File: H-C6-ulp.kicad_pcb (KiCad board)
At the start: 4 copper layers, 58.5 x 33 mm, 81 parts, among them IC1 W25Q80DVSSIG, J1 USB_C_Receptacle_USB2.0, J2 AFC24-S24FIC-00, J3 SM02B-SRSS-TB(LF)(SN), J4 SM04B-SRSS-TB_LF__SN_, J5 OLED, Q1 Si1308, Q2 Si2301CDS, SW1 SW_Push_Dual, SW2 SW_Push_Dual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

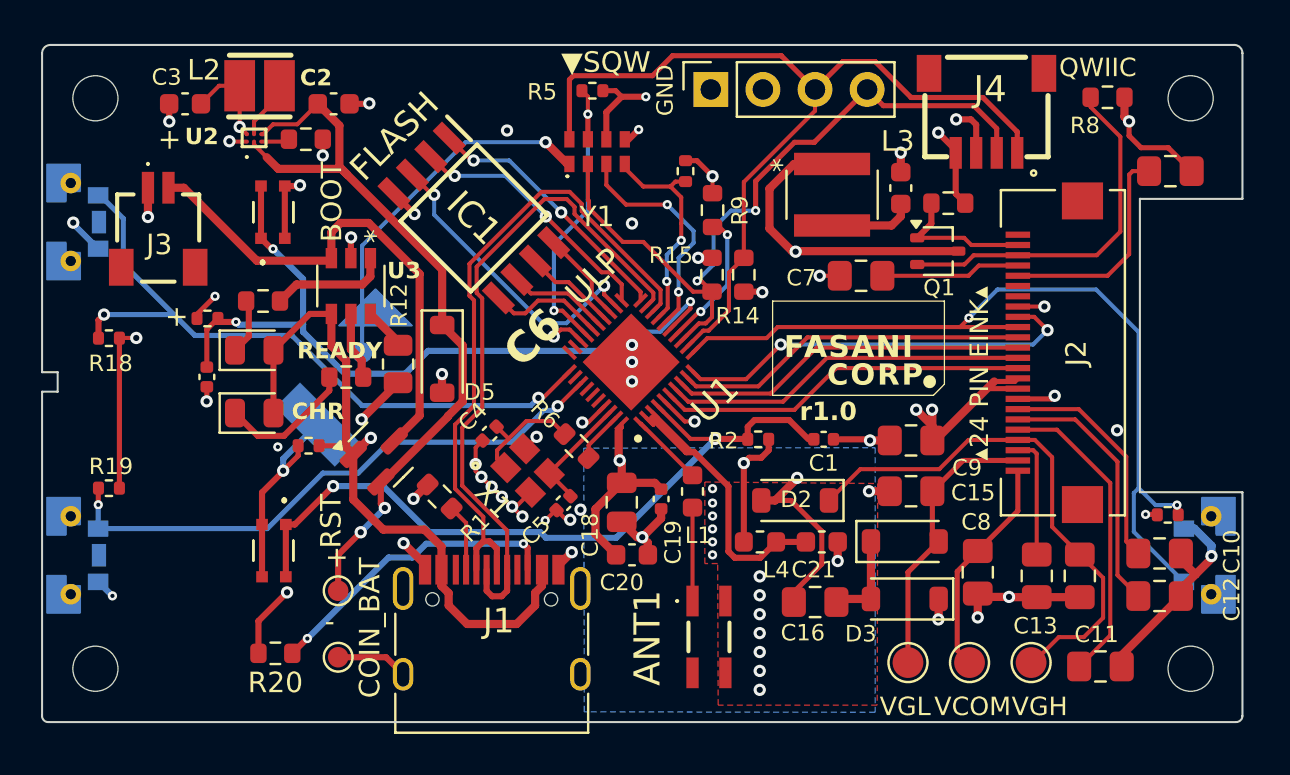
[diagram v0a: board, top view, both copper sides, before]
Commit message: Test with external flash
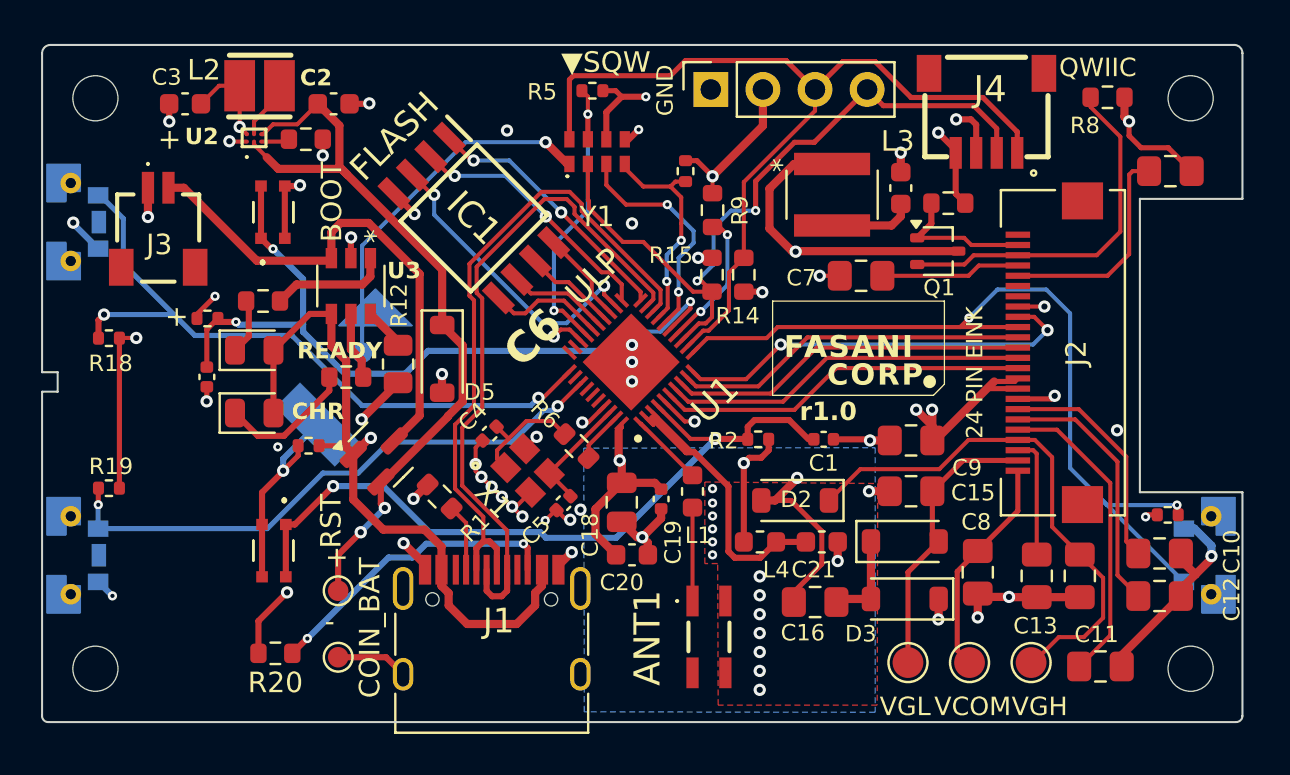
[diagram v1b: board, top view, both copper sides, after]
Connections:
- J5 pad 2: +3.3V -> VDD33
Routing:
- net VDD33: track 99.4 -> 104.8 mm
- net +3.3V: track 5.10 -> 0.00 mm
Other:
- board text added: "24 PIN EINK"
- board text removed: "▴24 PIN EINK▴"

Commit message: 1.1 ready for review
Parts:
- removed IC1: W25Q80DVSSIG, footprints:SOIC127P790X216-8N-FLASH
- removed R5: 10 K, Resistor_SMD:R_0402_1005Metric
- removed TP4: COIN BAT +, TestPoint:TestPoint_Pad_D1.0mm
- removed TP5: COIN BAT -, TestPoint:TestPoint_Pad_D1.0mm
- added TP10: RX, TestPoint:TestPoint_Pad_D1.0mm, F.Cu at (127.7, 49.3)
- added TP6: 21, TestPoint:TestPoint_Pad_D1.0mm, F.Cu at (117.0, 68.0)
- added TP7: 22, TestPoint:TestPoint_Pad_D1.0mm, F.Cu at (117.0, 71.6)
- added TP8: 23, TestPoint:TestPoint_Pad_D1.0mm, F.Cu at (117.0, 75.2)
- added TP9: TX, TestPoint:TestPoint_Pad_D1.0mm, F.Cu at (130.2, 49.3)
- U1: value ESP32-C6 -> ESP32-C6FH4; footprint footprints:C6_QFN40P500X500X90-41N-D -> Package_DFN_QFN:QFN-32-1EP_5x5mm_P0.5mm_EP3.6x3.6mm
- moved U1 0.48 mm to (138.5, 63.5)
- moved R6 0.28 mm to (135.8, 67.3)
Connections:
- R19 pad 1: SW20 -> SW19
- U1 pad 16: /RTC_INT -> /USB_D-
- U1 pad 17: /RTC_EVI -> /USB_D+
- U1 pad 18: /USB_D- -> /RTC_EVI
- U1 pad 19: /USB_D+ -> /RTC_INT
- U1 pad 20: SPICS0 -> VDD33
- U1 pad 21: SPI_D1 -> /IO_TX
- U1 pad 22: SPI_D2 -> /IO_RX
- U1 pad 23: SPIVDD -> SW18
- U1 pad 24: SPI_D3 -> SW19
- U1 pad 25: SPICLK -> /RTC_SQW
- U1 pad 26: SPI_D0 -> /IO_21
- U1 pad 27: /RTC_SQW -> /IO_22
- U1 pad 28: VDD33 -> /IO_23
- U1 pad 29: unconnected-(U1-U0TXD/GPIO16/FSPICS0-Pad29) -> VDD33
- U1 pad 30: unconnected-(U1-U0RXD/GPIO17/FSPICS1-Pad30) -> Net-(U1-XTAL_N)
- U1 pad 31: SW18 -> Net-(U1-XTAL_P)
- U1 pad 32: unconnected-(U1-GPIO19/SDIO_CLK/FSPICS3-Pad32) -> VDD33
- U1 pad 33: SW20 -> GND
- U6 pad 2: SW20 -> SW19
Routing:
- net SW19: track 0.00 -> 30.5 mm, vias 0 -> 2
- net SW20: track 28.5 -> 0.00 mm, vias 2 -> 0
- net /IO_23: track 0.00 -> 23.9 mm, vias 0 -> 2
- net /IO_22: track 0.00 -> 22.3 mm, vias 0 -> 2
- net /IO_21: track 0.00 -> 21.5 mm, vias 0 -> 2
- net /IO_RX: track 0.00 -> 17.5 mm, vias 0 -> 2
- net /IO_TX: track 0.00 -> 15.9 mm, vias 0 -> 2
- net SPI_D2: track 14.9 -> 0.00 mm, vias 2 -> 0
- net SPICS0: track 12.8 -> 0.00 mm, vias 2 -> 0
- net SPI_D1: track 12.7 -> 0.00 mm, vias 2 -> 0
- net /RTC_SQW: track 14.9 -> 21.4 mm
- net VDD: track 37.9 -> 31.7 mm, vias 2 -> 0
- net SPI_D0: track 5.74 -> 0.00 mm
- net BOOT: track 37.8 -> 42.9 mm
- net SPICLK: track 4.87 -> 0.00 mm
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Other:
- board text added: "21"
- board text added: "22"
- board text added: "23"
- board text added: "RX 17"
- board text added: "Rev 1.1"
- board text added: "TX 16"
- board text removed: "-"
- board text removed: "COIN_BAT"
- board text removed: "FLASH"
- board text removed: "Rev 1.0"
- board text removed: "r1.0"

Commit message: Cleanup
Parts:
- moved R4 1.35 mm to (141.3, 55.1)
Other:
- board text removed: "▼SQW"
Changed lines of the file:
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@@
   )
   (footprint "Resistor_SMD:R_0402_1005Metric" (layer "F.Cu")
-    (at 141.36 53.75 -90)
+    (at 141.3 55.1 -90)
     (descr "Resistor SMD 0402 (1005 Metric), square (rectangular) end terminal, IPC_7351 nominal, (Body size source: IPC-SM-782 page 72, https://www.pcb-3d.com/wordpress/wp-content/uploads/ipc-sm-782a_amendment_1_and_2.pdf), generated with kicad-footprint-generator")
     (tags "resistor")
@@
     (effects (font (size 1 1) (thickness 0.1)) (justify left bottom))
   )
-  (gr_text "▼SQW" (at 135.3 49.03) (layer "F.SilkS" knockout)
-    (effects (font (size 1 1) (thickness 0.1)) (justify left bottom))
-  )
-  (gr_text "GND" (at 140.95 52.65) (layer "F.SilkS")
+  (gr_text "GND" (at 141.2 53.9 45) (layer "F.SilkS")
     (effects (font (size 0.8 0.8) (thickness 0.1)) (justify left bottom))
   )
@@
     (effects (font (size 1 1) (thickness 0.1)) (justify left bottom))
   )
-  (gr_text "3V3" (at 143.45 53.9 45) (layer "F.SilkS")
+  (gr_text "3V3" (at 143.2 53.9 45) (layer "F.SilkS")
     (effects (font (size 0.8 0.8) (thickness 0.1)) (justify left bottom))
   )
@@
   (segment (start 138.25 68.94) (end 139.86 68.94) (width 0.4) (layer "F.Cu") (net 6))
   (segment (start 144.2 67.98) (end 144.46 67.72) (width 0.3) (layer "F.Cu") (net 6))
-  (segment (start 141.915 53.24) (end 142.675 54) (width 0.25) (layer "F.Cu") (net 6))
   (segment (start 156.4 64) (end 157.4044 64) (width 0.25) (layer "F.Cu") (net 6))
   (segment (start 136.942893 65.392893) (end 136.457906 65.87788) (width 0.2) (layer "F.Cu") (net 6))
@@
   (segment (start 154.547702 51.227298) (end 155.267298 51.227298) (width 0.3) (layer "F.Cu") (net 6))
   (segment (start 119.98 51.95125) (end 119.98 51.94375) (width 0.2) (layer "F.Cu") (net 6))
+  (segment (start 142.675 54.825) (end 141.535 54.825) (width 0.2) (layer "F.Cu") (net 6))
   (segment (start 136.924517 61.574517) (end 134.45 59.1) (width 0.25) (layer "F.Cu") (net 6))
   (segment (start 137.85 66.607106) (end 138.003553 66.453553) (width 0.2) (layer "F.Cu") (net 6))
   (segment (start 138.15 67.85) (end 138.15 67.55) (width 0.4) (layer "F.Cu") (net 6))
-  (segment (start 141.36 53.24) (end 141.915 53.24) (width 0.25) (layer "F.Cu") (net 6))
   (segment (start 153.3875 66.875) (end 153.3875 65.3875) (width 0.4) (layer "F.Cu") (net 6))
   (segment (start 144.2 59.625) (end 145.075 59.625) (width 0.3) (layer "F.Cu") (net 6))
@@
   (segment (start 164.35 70.5) (end 163.88 70.5) (width 0.25) (layer "F.Cu") (net 6))
   (segment (start 163.88 70.5) (end 163.78 70.6) (width 0.25) (layer "F.Cu") (net 6))
+  (segment (start 141.535 54.825) (end 141.3 54.59) (width 0.2) (layer "F.Cu") (net 6))
   (segment (start 144.46 67.72) (end 145.045 67.72) (width 0.3) (layer "F.Cu") (net 6))
   (segment (start 153.525 66.875) (end 156.4 64) (width 0.4) (layer "F.Cu") (net 6))
@@
   (segment (start 120.68 52.31125) (end 121.9125 52.31125) (width 0.2) (layer "F.Cu") (net 48))
   (segment (start 138.4 55.2) (end 137.75 55.85) (width 0.25) (layer "F.Cu") (net 49))
+  (segment (start 138.4 53.6) (end 140.41 55.61) (width 0.2) (layer "F.Cu") (net 49))
   (segment (start 136.3 57.4) (end 136.3 59.51741) (width 0.25) (layer "F.Cu") (net 49))
-  (segment (start 139.3 54.5) (end 138.4 53.6) (width 0.2) (layer "F.Cu") (net 49))
+  (segment (start 140.41 55.61) (end 141.3 55.61) (width 0.2) (layer "F.Cu") (net 49))
   (segment (start 136.3 59.51741) (end 137.65 60.86741) (width 0.25) (layer "F.Cu") (net 49))
-  (segment (start 140.625 54.5) (end 140.865 54.26) (width 0.2) (layer "F.Cu") (net 49))
-  (segment (start 140.865 54.26) (end 141.36 54.26) (width 0.2) (layer "F.Cu") (net 49))
-  (segment (start 140.625 54.5) (end 139.3 54.5) (width 0.2) (layer "F.Cu") (net 49))
   (segment (start 138.4 53.4) (end 138.4 55.2) (width 0.25) (layer "F.Cu") (net 49))
   (via (at 137.75 55.85) (size 0.6) (drill 0.3) (layers "F.Cu" "B.Cu") (net 49))

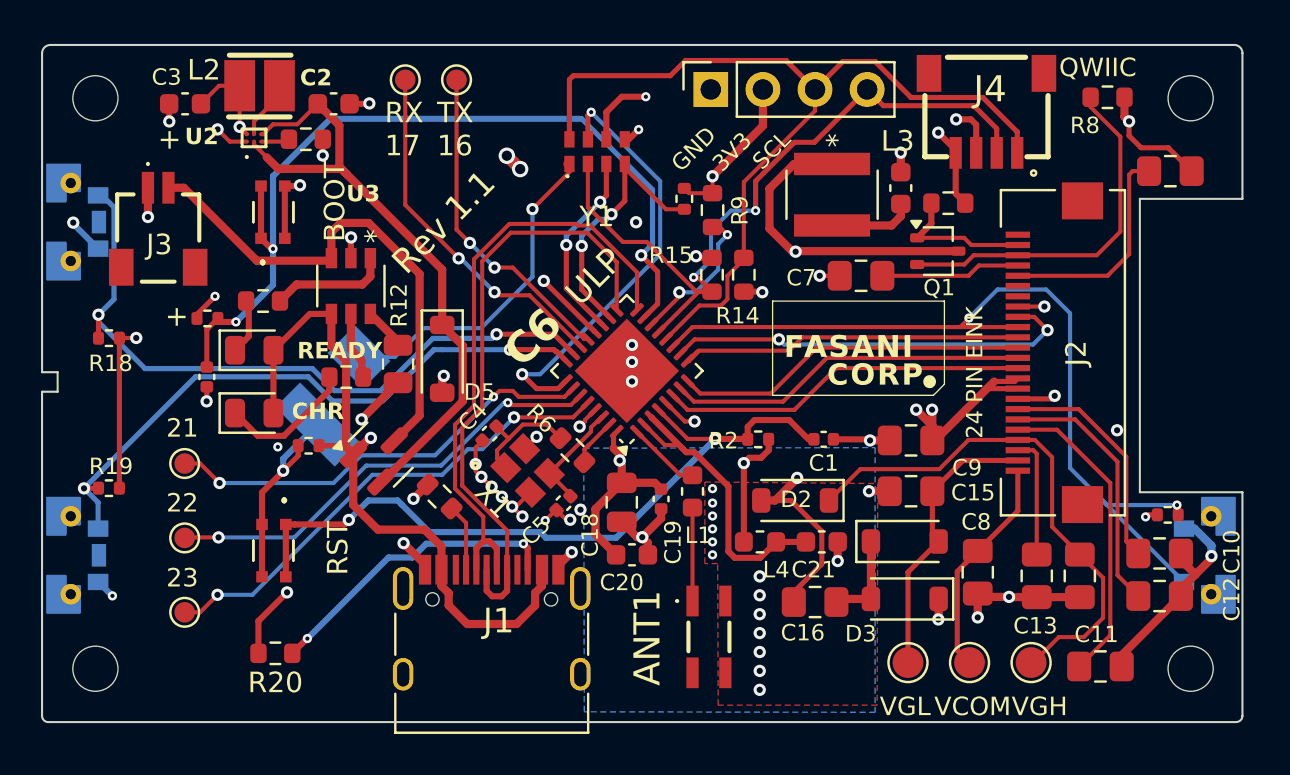
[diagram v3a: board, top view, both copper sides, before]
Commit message: Saving 1.1 state before making it 51 mm
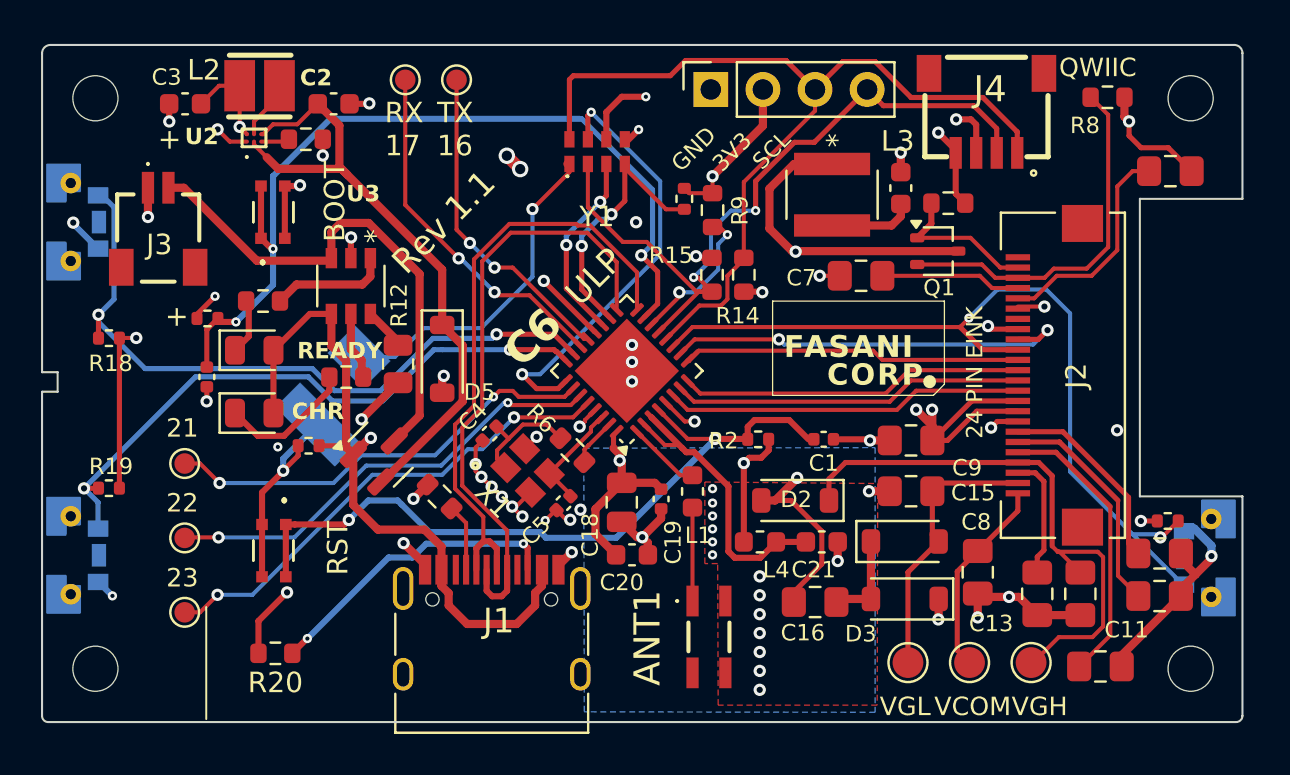
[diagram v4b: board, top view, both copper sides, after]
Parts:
- moved J2 1.10 mm to (159.8, 63.7)
- moved C13 0.88 mm to (158.5, 74.3)
- moved C14 0.88 mm to (160.6, 74.3)
- moved R17 0.30 mm to (164.9, 70.8)
- moved U5 0.13 mm to (166.5, 72.6)
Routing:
- net VDD33: track 107.4 -> 110.0 mm
- net Net-(C10-Pad2): track 11.2 -> 8.98 mm
- net PREVGH: track 25.8 -> 27.8 mm
- net Net-(C12-Pad2): track 12.7 -> 11.1 mm
- net unconnected-(J2-Pad19): track 0.00 -> 1.30 mm, vias 0 -> 1
- net /EPD_RST: track 43.6 -> 42.4 mm
- net Net-(C11-Pad2): track 15.2 -> 14.0 mm
- net /VCOM: track 10.8 -> 9.72 mm
- net Net-(D1-A): track 13.9 -> 12.9 mm
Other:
- outline, holes or cut-outs redrawn

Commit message: Rel 1.1 ready
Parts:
- R7: footprint Resistor_SMD:R_0603_1608Metric -> Resistor_SMD:R_0402_1005Metric
- moved SW2 17.2 mm to (118.2, 72.7), turned to -90 degrees
- moved R18 12.9 mm to (121.5, 52.0)
- moved TP6 10.5 mm to (123.3, 76.3)
- moved C2 10.0 mm to (129.6, 58.9), turned to -90 degrees
- moved TP7 8.80 mm to (121.9, 78.9)
- moved TP8 8.70 mm to (124.8, 78.9)
- moved C3 7.34 mm to (124.3, 50.8), turned to 90 degrees
- moved L2 6.88 mm to (127.4, 50.5)
- moved R3 6.88 mm to (129.7, 53.1)
- moved U2 6.88 mm to (127.2, 53.0)
- moved R16 6.01 mm to (119.3, 66.8), turned to 90 degrees
- moved H1 5.40 mm to (118.0, 50.2)
- moved H3 5.40 mm to (118.0, 78.0)
- moved U4 5.08 mm to (117.0, 55.6)
- moved U6 5.08 mm to (117.0, 71.9)
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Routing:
- net VDD33: track 110.0 -> 97.2 mm, vias 21 -> 18
- net BOOT: track 42.9 -> 52.8 mm, vias 3 -> 2
- net VDD: track 31.7 -> 24.4 mm
- net VBUS: track 40.1 -> 47.0 mm
- net GND: track 84.7 -> 90.0 mm, vias 57 -> 55
- net SW19: track 30.5 -> 25.6 mm
- net Net-(J1-CC2): track 14.8 -> 10.9 mm
- net SW18: track 34.1 -> 36.3 mm
- net VBAT: track 24.9 -> 22.8 mm
- net /IO_22: track 22.3 -> 24.4 mm
- net Net-(D6-K): track 6.62 -> 8.71 mm
- net Net-(D4-K): track 2.73 -> 4.15 mm
- net /IO_RX: track 17.5 -> 16.2 mm
- net ENABLE: track 35.3 -> 34.3 mm
- net Net-(U3-*STDBY): track 2.96 -> 2.26 mm
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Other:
- board size 58.5 x 33 mm -> 53.5 x 33 mm
- board text added: "1.1"
- board text added: "16"
- board text added: "17"
- board text added: "21▶"
- board text added: "CHARGE"
- board text added: "RTC"
- board text removed: "21"
- board text removed: "CHR"
- board text removed: "RX 17"
- board text removed: "Rev 1.1"
- board text removed: "TX 16"

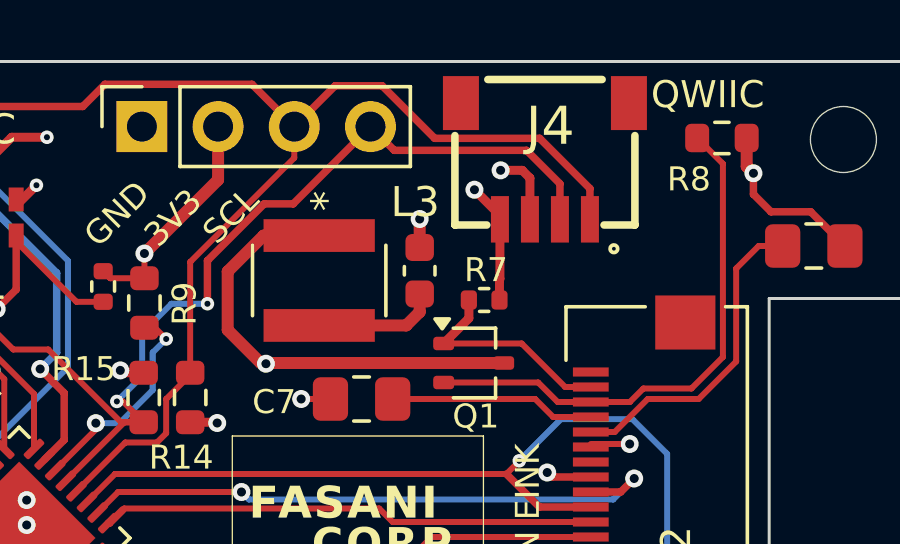
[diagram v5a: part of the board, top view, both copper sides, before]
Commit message: Fix epaper power
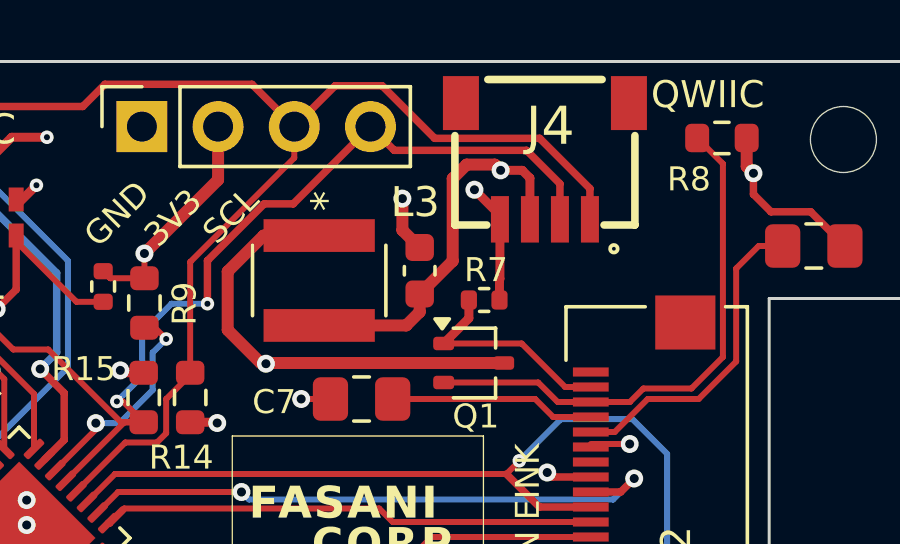
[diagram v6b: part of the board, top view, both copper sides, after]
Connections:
- C17 pad 2: +3V3 -> VDD33
- L3 pad 2: +3V3 -> VDD33
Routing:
- net VDD33: track 97.2 -> 107.5 mm
- net +3V3: track 4.14 -> 0.00 mm
- net GND: track 90.0 -> 90.9 mm
